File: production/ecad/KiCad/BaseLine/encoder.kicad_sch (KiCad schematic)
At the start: 10 parts, among them J5 Rotary Encoder Connector, U9 TXB0104DR

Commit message: fixed level shifters
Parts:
- added C31, C32: 0.1u, symbol Device:C
- R40: value 10k -> DNP
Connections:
- net +3.3V: now also C31.1; no longer U9.1 (VCCA)
- net +5V: now also C32.1; no longer U9.14 (VCCB)
- new net: C32.2, U9.14 (VCCB)
- new net: C31.2, U9.1 (VCCA)
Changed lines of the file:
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@@
+	(wire
+		(pts
+			(xy 106.68 52.07) (xy 106.68 53.34)
+		)
+		(stroke
+			(width 0)
+			(type default)
+		)
+	)
 	(wire
 		(pts
@@
 	(wire
 		(pts
+			(xy 114.3 41.91) (xy 114.3 44.45)
+		)
+		(stroke
+			(width 0)
+			(type default)
+		)
+	)
+	(wire
+		(pts
+			(xy 106.68 41.91) (xy 106.68 44.45)
+		)
+		(stroke
+			(width 0)
+			(type default)
+		)
+	)
+	(wire
+		(pts
 			(xy 115.57 60.96) (xy 124.46 60.96)
 		)
@@
 	(wire
 		(pts
-			(xy 106.68 53.34) (xy 106.68 48.26)
-		)
-		(stroke
-			(width 0)
-			(type default)
-		)
-	)
-	(wire
-		(pts
 			(xy 64.77 71.12) (xy 68.58 71.12)
 		)
@@
 	(wire
 		(pts
-			(xy 104.14 55.88) (xy 113.03 55.88)
+			(xy 104.14 55.88) (xy 114.3 55.88)
 		)
 		(stroke
@@
 	(wire
 		(pts
-			(xy 113.03 55.88) (xy 113.03 48.26)
-		)
-		(stroke
-			(width 0)
-			(type default)
-		)
-	)
-	(wire
-		(pts
 			(xy 55.88 66.04) (xy 63.5 66.04)
 		)
@@
 		(pts
 			(xy 104.14 78.74) (xy 106.68 78.74)
+		)
+		(stroke
+			(width 0)
+			(type default)
+		)
+	)
+	(wire
+		(pts
+			(xy 114.3 52.07) (xy 114.3 55.88)
 		)
 		(stroke
@@
 			)
 		)
-		(property "Value" "10k"
+		(property "Value" "DNP"
 			(at 67.31 78.7399 0)
 			(effects
@@
 	(symbol
 		(lib_id "power:+5V")
-		(at 113.03 48.26 0)
+		(at 114.3 41.91 0)
 		(unit 1)
 		(exclude_from_sim no)
@@
 		(fields_autoplaced yes)
 		(property "Reference" "#PWR066"
-			(at 113.03 52.07 0)
+			(at 114.3 45.72 0)
 			(effects
 				(font
@@
 		)
 		(property "Value" "+5V"
-			(at 113.03 43.18 0)
+			(at 114.3 36.83 0)
 			(effects
 				(font
@@
 		)
 		(property "Footprint" ""
-			(at 113.03 48.26 0)
+			(at 114.3 41.91 0)
 			(effects
 				(font
@@
 		)
 		(property "Datasheet" ""
-			(at 113.03 48.26 0)
+			(at 114.3 41.91 0)
 			(effects
 				(font
@@
 		)
 		(property "Description" "Power symbol creates a global label with name \"+5V\""
-			(at 113.03 48.26 0)
+			(at 114.3 41.91 0)
 			(effects
 				(font
@@
 	(symbol
 		(lib_id "power:+3.3V")
-		(at 106.68 48.26 0)
+		(at 106.68 41.91 0)
 		(unit 1)
 		(exclude_from_sim no)
@@
 		(fields_autoplaced yes)
 		(property "Reference" "#PWR064"
-			(at 106.68 52.07 0)
+			(at 106.68 45.72 0)
 			(effects
 				(font
@@
 		)
 		(property "Value" "+3.3V"
-			(at 106.68 43.18 0)
+			(at 106.68 36.83 0)
 			(effects
 				(font
@@
 		)
 		(property "Footprint" ""
-			(at 106.68 48.26 0)
+			(at 106.68 41.91 0)
 			(effects
 				(font
@@
 		)
 		(property "Datasheet" ""
-			(at 106.68 48.26 0)
+			(at 106.68 41.91 0)
 			(effects
 				(font
@@
 		)
 		(property "Description" "Power symbol creates a global label with name \"+3.3V\""
-			(at 106.68 48.26 0)
+			(at 106.68 41.91 0)
 			(effects
 				(font
@@
 	)
 	(symbol
+		(lib_id "Device:C")
+		(at 114.3 48.26 0)
+		(unit 1)
+		(exclude_from_sim no)
+		(in_bom yes)
+		(on_board yes)
+		(dnp no)
+		(property "Reference" "C32"
+			(at 116.586 44.704 0)
+			(effects
+				(font
+					(size 1.27 1.27)
+				)
+				(justify left)
+			)
+		)
+		(property "Value" "0.1u"
+			(at 118.11 47.752 0)
+			(effects
+				(font
+					(size 1.27 1.27)
+				)
+				(justify left)
+			)
+		)
+		(property "Footprint" ""
+			(at 115.2652 52.07 0)
+			(effects
+				(font
+					(size 1.27 1.27)
+				)
+				(hide yes)
+			)
+		)
+		(property "Datasheet" "~"
+			(at 114.3 48.26 0)
+			(effects
+				(font
+					(size 1.27 1.27)
+				)
+				(hide yes)
+			)
+		)
+		(property "Description" "Unpolarized capacitor"
+			(at 114.3 48.26 0)
+			(effects
+				(font
+					(size 1.27 1.27)
+				)
+				(hide yes)
+			)
+		)
+		(pin "2"
+		)
+		(pin "1"
+		)
+		(instances
+			(project "BaseLine"
+				(path "/ba9eda21-3882-41e1-8265-3d8ac781da20/83d2619d-438a-45a6-9609-f1b511caf8bd"
+					(reference "C32")
+					(unit 1)
+				)
+			)
+		)
+	)
+	(symbol
 		(lib_id "TXB0104DR:TXB0104DR")
 		(at 86.36 66.04 0)
@@
 					(unit 1)
 				)
+			)
+		)
+	)
+	(symbol
+		(lib_id "Device:C")
+		(at 106.68 48.26 0)
+		(unit 1)
+		(exclude_from_sim no)
+		(in_bom yes)
+		(on_board yes)
+		(dnp no)
+		(property "Reference" "C31"
+			(at 100.838 44.704 0)
+			(effects
+				(font
+					(size 1.27 1.27)
+				)
+				(justify left)
+			)
+		)
+		(property "Value" "0.1u"
+			(at 99.568 47.498 0)
+			(effects
+				(font
+					(size 1.27 1.27)
+				)
+				(justify left)
+			)
+		)
+		(property "Footprint" ""
+			(at 107.6452 52.07 0)
+			(effects
+				(font
+					(size 1.27 1.27)
+				)
+				(hide yes)
+			)
+		)
+		(property "Datasheet" "~"
+			(at 106.68 48.26 0)
+			(effects
+				(font
+					(size 1.27 1.27)
+				)
+				(hide yes)
+			)
+		)
+		(property "Description" "Unpolarized capacitor"
+			(at 106.68 48.26 0)
+			(effects
+				(font
+					(size 1.27 1.27)
+				)
+				(hide yes)
+			)
+		)
+		(pin "2"
+		)
+		(pin "1"
+		)
+		(instances
+			(project ""
+				(path "/ba9eda21-3882-41e1-8265-3d8ac781da20/83d2619d-438a-45a6-9609-f1b511caf8bd"
+					(reference "C31")
+					(unit 1)
+				)

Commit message: add footprints
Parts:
- C31, C32: footprint (none) -> Capacitor_SMD:C_0805_2012Metric_Pad1.18x1.45mm_HandSolder
- R39, R40: footprint (none) -> Resistor_SMD:R_0805_2012Metric_Pad1.20x1.40mm_HandSolder
- TP14, TP15, TP16, TP17, TP18, TP19: footprint (none) -> TestPoint:TestPoint_Pad_D1.5mm
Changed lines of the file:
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@@
 			)
 		)
-		(property "Footprint" ""
+		(property "Footprint" "TestPoint:TestPoint_Pad_D1.5mm"
 			(at 68.58 66.04 0)
 			(effects
@@
 			)
 		)
-		(property "Footprint" ""
+		(property "Footprint" "TestPoint:TestPoint_Pad_D1.5mm"
 			(at 63.5 60.96 0)
 			(effects
@@
 			)
 		)
-		(property "Footprint" ""
+		(property "Footprint" "Resistor_SMD:R_0805_2012Metric_Pad1.20x1.40mm_HandSolder"
 			(at 64.77 77.47 0)
 			(effects
@@
 			)
 		)
-		(property "Footprint" ""
+		(property "Footprint" "TestPoint:TestPoint_Pad_D1.5mm"
 			(at 66.04 63.5 0)
 			(effects
@@
 			)
 		)
-		(property "Footprint" ""
+		(property "Footprint" "TestPoint:TestPoint_Pad_D1.5mm"
 			(at 125.73 66.04 0)
 			(effects
@@
 			)
 		)
-		(property "Footprint" ""
+		(property "Footprint" "TestPoint:TestPoint_Pad_D1.5mm"
 			(at 123.19 63.5 0)
 			(effects
@@
 			)
 		)
-		(property "Footprint" ""
+		(property "Footprint" "Resistor_SMD:R_0805_2012Metric_Pad1.20x1.40mm_HandSolder"
 			(at 49.53 71.12 0)
 			(effects
@@
 			)
 		)
-		(property "Footprint" ""
+		(property "Footprint" "Capacitor_SMD:C_0805_2012Metric_Pad1.18x1.45mm_HandSolder"
 			(at 115.2652 52.07 0)
 			(effects
@@
 			)
 		)
-		(property "Footprint" ""
+		(property "Footprint" "TestPoint:TestPoint_Pad_D1.5mm"
 			(at 120.65 60.96 0)
 			(effects
@@
 			)
 		)
-		(property "Footprint" ""
+		(property "Footprint" "Capacitor_SMD:C_0805_2012Metric_Pad1.18x1.45mm_HandSolder"
 			(at 107.6452 52.07 0)
 			(effects

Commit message: pulldowns on lvl shifter
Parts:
- added R33, R57: 75k, Resistor_SMD:R_0805_2012Metric_Pad1.20x1.40mm_HandSolder, symbol Device:R_Small_US
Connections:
- net GND: now also R33.1, R57.1
- net at U9.10 (B4): now also R57.2
- net at U9.5 (A4): now also R33.2
- no-connect marks 2 -> 0
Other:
- moved on the sheet: R39, R40

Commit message: Test point footprints changed
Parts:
- TP14, TP15, TP16, TP17, TP18, TP19: footprint TestPoint:TestPoint_Pad_D1.5mm -> TestPoint:TestPoint_Pad_2.0x2.0mm
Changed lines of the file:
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@@
 			)
 		)
-		(property "Footprint" "TestPoint:TestPoint_Pad_D1.5mm"
+		(property "Footprint" "TestPoint:TestPoint_Pad_2.0x2.0mm"
 			(at 68.58 66.04 0)
 			(effects
@@
 			)
 		)
-		(property "Footprint" "TestPoint:TestPoint_Pad_D1.5mm"
+		(property "Footprint" "TestPoint:TestPoint_Pad_2.0x2.0mm"
 			(at 63.5 60.96 0)
 			(effects
@@
 			)
 		)
-		(property "Footprint" "TestPoint:TestPoint_Pad_D1.5mm"
+		(property "Footprint" "TestPoint:TestPoint_Pad_2.0x2.0mm"
 			(at 66.04 63.5 0)
 			(effects
@@
 			)
 		)
-		(property "Footprint" "TestPoint:TestPoint_Pad_D1.5mm"
+		(property "Footprint" "TestPoint:TestPoint_Pad_2.0x2.0mm"
 			(at 125.73 66.04 0)
 			(effects
@@
 			)
 		)
-		(property "Footprint" "TestPoint:TestPoint_Pad_D1.5mm"
+		(property "Footprint" "TestPoint:TestPoint_Pad_2.0x2.0mm"
 			(at 123.19 63.5 0)
 			(effects
@@
 			)
 		)
-		(property "Footprint" "TestPoint:TestPoint_Pad_D1.5mm"
+		(property "Footprint" "TestPoint:TestPoint_Pad_2.0x2.0mm"
 			(at 120.65 60.96 0)
 			(effects

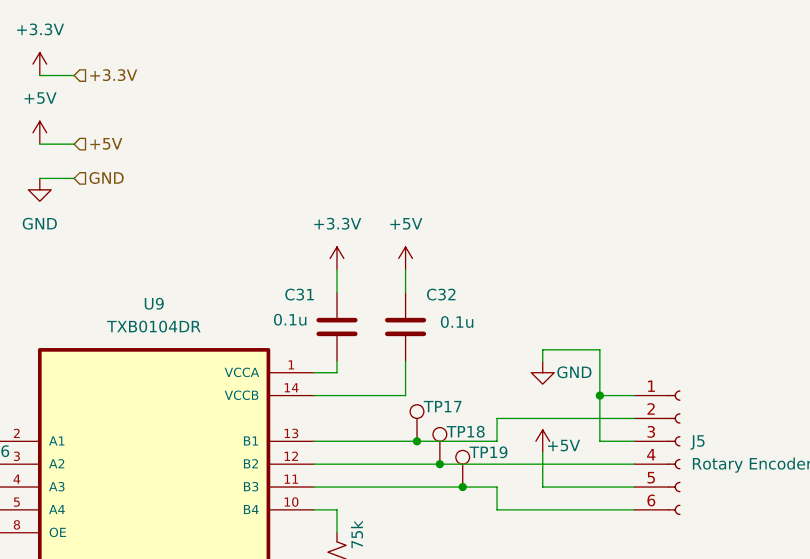
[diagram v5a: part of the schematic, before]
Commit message: fixed lvl shifter power
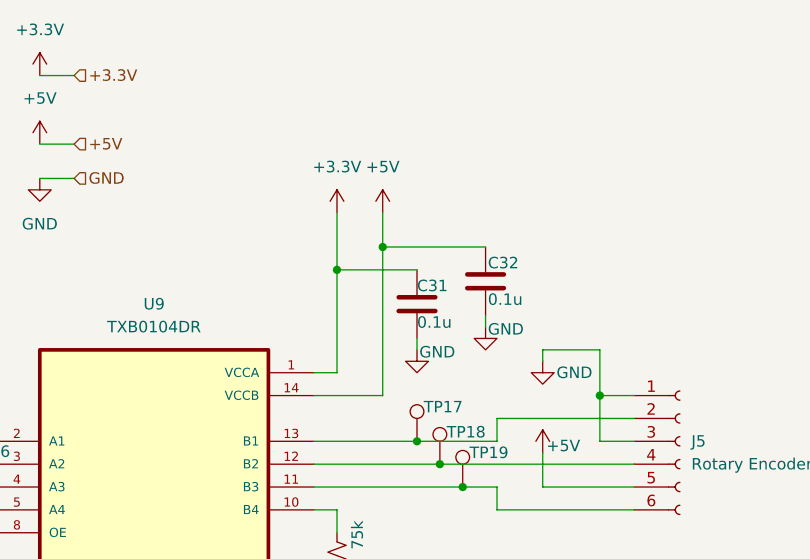
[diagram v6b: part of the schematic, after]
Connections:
- net +3.3V: now also U9.1 (VCCA)
- net +5V: now also U9.14 (VCCB)
- net GND: now also C31.2, C32.2
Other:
- moved on the sheet: C31, C32

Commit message: doing some things for layout
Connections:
- net +3.3V: now also C31.2; no longer C31.1
- net GND: now also C31.1; no longer C31.2
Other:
- moved on the sheet: C31, C32
